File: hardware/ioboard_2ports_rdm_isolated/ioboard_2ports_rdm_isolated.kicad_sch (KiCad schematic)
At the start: 30 parts, among them J1 Conn_02x06_Odd_Even, J12 Conn_01x03, J2 XLR3, J3 XLR3, J6 Conn_01x03, J8 XLR3, J9 XLR3, U1 M24C64-RMN6TP, U2 CRE1S0505DC, U4 ADM2483xRW, U6 ADM2483xRW

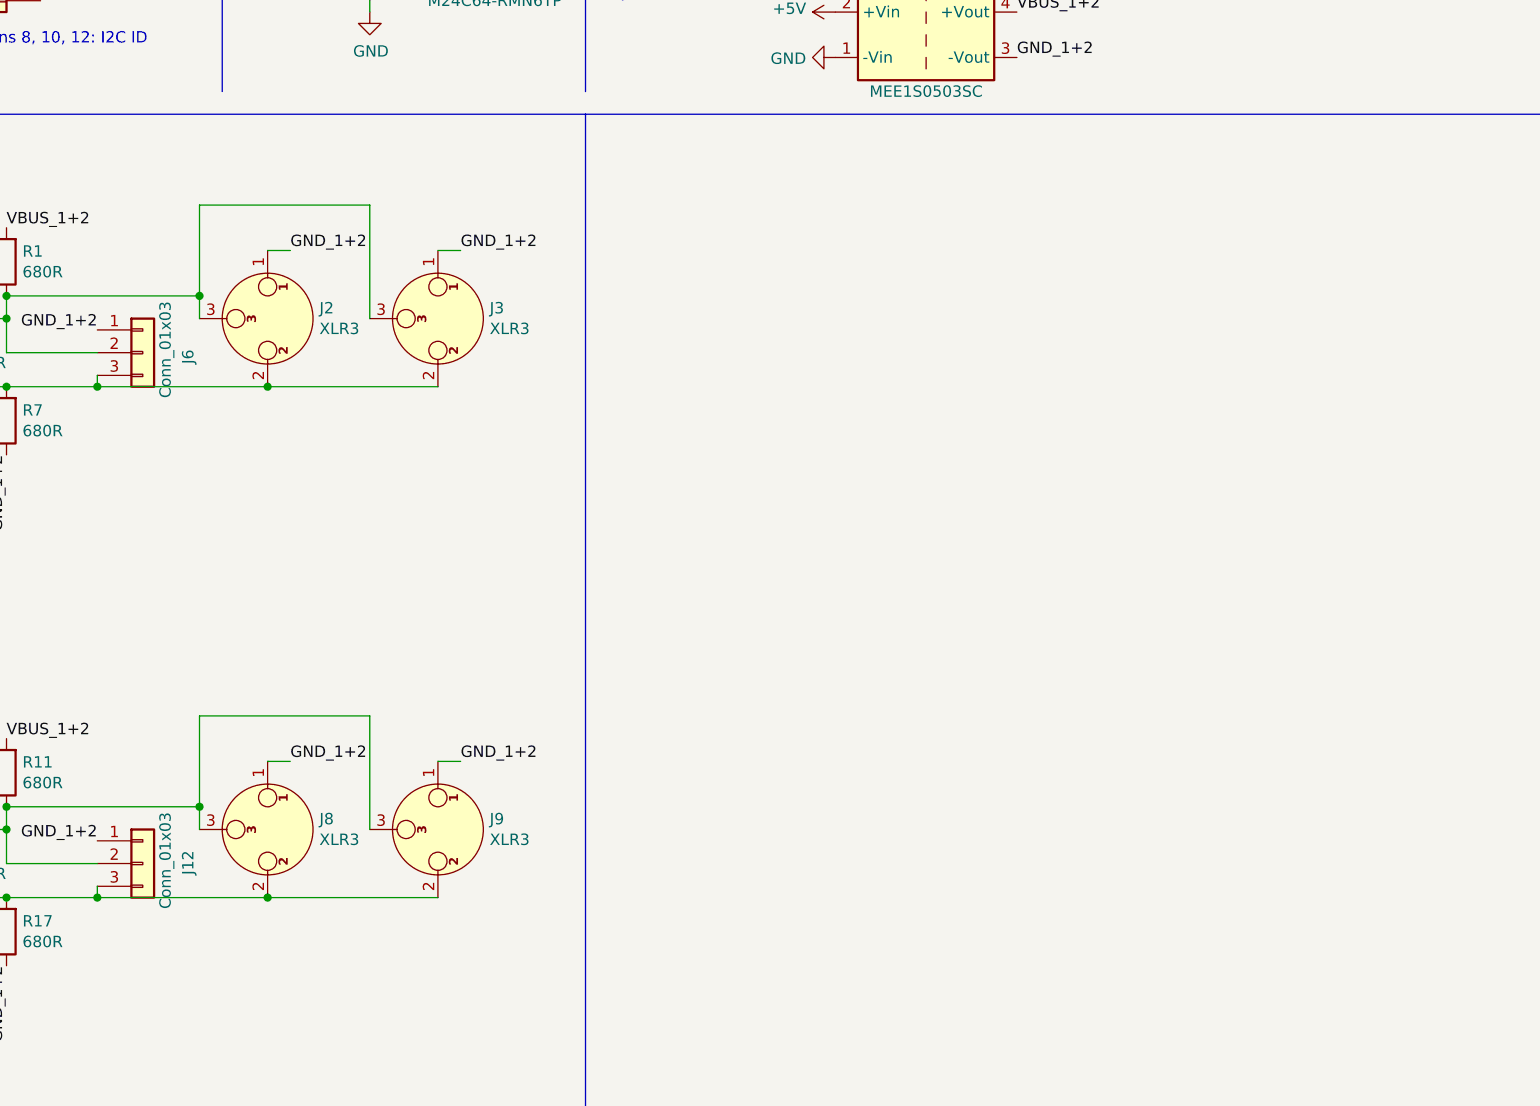
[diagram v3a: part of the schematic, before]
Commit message: Add an RJ45 connector to ioboard_2ports_rdm_isolated
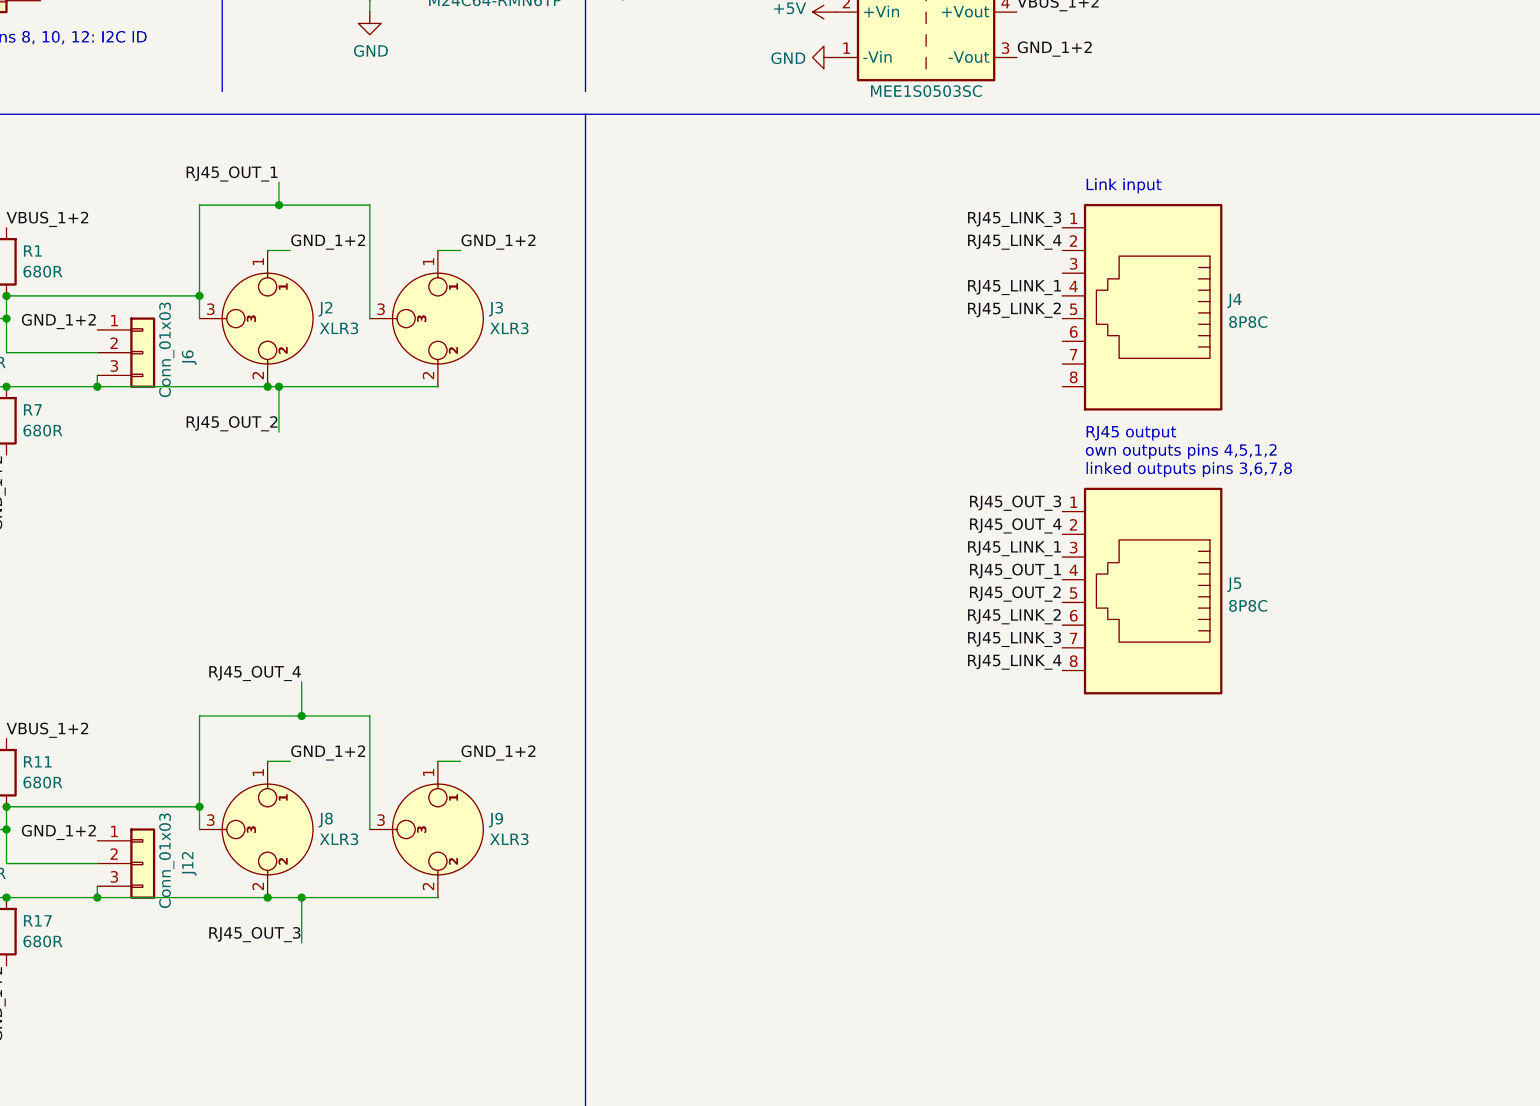
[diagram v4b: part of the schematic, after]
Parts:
- added J4, J5: 8P8C, Connector_RJ:RJ45_Amphenol_RJHSE5380, symbol Connector:8P8C
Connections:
- net RJ45_OUT_1: now reaches J2.3, J3.3, J6.2 (Pin_2), R1.1, R5.2, U4.12 (A)
- net RJ45_OUT_1: now also J5.4
- net RJ45_OUT_2: now reaches J2.2, J3.2, J6.3 (Pin_3), R5.1, R7.2, U4.13 (B)
- net RJ45_OUT_2: now also J5.5
- net RJ45_OUT_3: now reaches J12.3 (Pin_3), J8.2, J9.2, R15.1, R17.2, U6.13 (B)
- net RJ45_OUT_3: now also J5.1
- net RJ45_OUT_4: now reaches J12.2 (Pin_2), J8.3, J9.3, R11.1, R15.2, U6.12 (A)
- net RJ45_OUT_4: now also J5.2
- new net RJ45_LINK_1: J4.4, J5.3
- new net RJ45_LINK_2: J4.5, J5.6
- new net RJ45_LINK_3: J4.1, J5.7
- new net RJ45_LINK_4: J4.2, J5.8
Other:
- note added: "Link input"
- note added: "RJ45 output own outputs pins 4,5,1,2 linked outputs pins 3,6,7,8"
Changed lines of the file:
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@@
     (title "rp2040_dongle_ioboard_2ports_rdm_isolated")
     (date "2022-11-09")
-    (rev "0.5")
+    (rev "0.6")
     (company "https://www.openlighting.org")
   )
   (junction (at 105.41 73.66) (diameter 0) (color 0 0 0 0)
   )
+  (junction (at 114.3 83.82) (diameter 0) (color 0 0 0 0)
+  )
   (junction (at 113.03 83.82) (diameter 0) (color 0 0 0 0)
   )
@@
   (junction (at 45.72 64.77) (diameter 0) (color 0 0 0 0)
   )
+  (junction (at 114.3 63.5) (diameter 0) (color 0 0 0 0)
+  )
   (junction (at 29.21 139.7) (diameter 0) (color 0 0 0 0)
   )
@@
   (junction (at 77.47 83.82) (diameter 0) (color 0 0 0 0)
   )
+  (junction (at 116.84 140.97) (diameter 0) (color 0 0 0 0)
+  )
   (junction (at 83.82 73.66) (diameter 0) (color 0 0 0 0)
   )
@@
   (junction (at 83.82 83.82) (diameter 0) (color 0 0 0 0)
   )
+  (junction (at 116.84 120.65) (diameter 0) (color 0 0 0 0)
+  )
   (junction (at 45.72 121.92) (diameter 0) (color 0 0 0 0)
   )
@@
     (stroke (width 0) (type default) (color 0 0 0 0))
   )
-  (wire (pts (xy 105.41 120.65) (xy 124.46 120.65))
+  (wire (pts (xy 105.41 120.65) (xy 116.84 120.65))
     (stroke (width 0) (type default) (color 0 0 0 0))
   )
@@
     (stroke (width 0) (type default) (color 0 0 0 0))
   )
-  (wire (pts (xy 105.41 63.5) (xy 124.46 63.5))
+  (wire (pts (xy 105.41 63.5) (xy 114.3 63.5))
     (stroke (width 0) (type default) (color 0 0 0 0))
   )
@@
     (stroke (width 0) (type default) (color 0 0 0 0))
   )
+  (wire (pts (xy 116.84 140.97) (xy 132.08 140.97))
+    (stroke (width 0) (type default) (color 0 0 0 0))
+  )
   (wire (pts (xy 66.04 134.62) (xy 71.12 134.62))
     (stroke (width 0) (type default) (color 0 0 0 0))
@@
     (stroke (width 0) (type default) (color 0 0 0 0))
   )
+  (wire (pts (xy 116.84 116.84) (xy 116.84 120.65))
+    (stroke (width 0) (type default) (color 0 0 0 0))
+  )
   (wire (pts (xy 24.13 72.39) (xy 21.59 72.39))
     (stroke (width 0) (type default) (color 0 0 0 0))
   )
+  (wire (pts (xy 114.3 83.82) (xy 114.3 88.9))
+    (stroke (width 0) (type default) (color 0 0 0 0))
+  )
   (wire (pts (xy 124.46 63.5) (xy 124.46 76.2))
     (stroke (width 0) (type default) (color 0 0 0 0))
@@
     (stroke (width 0) (type default) (color 0 0 0 0))
   )
+  (wire (pts (xy 116.84 120.65) (xy 124.46 120.65))
+    (stroke (width 0) (type default) (color 0 0 0 0))
+  )
   (wire (pts (xy 173.99 24.13) (xy 173.99 22.86))
     (stroke (width 0) (type default) (color 0 0 0 0))
@@
     (stroke (width 0) (type default) (color 0 0 0 0))
   )
+  (wire (pts (xy 114.3 83.82) (xy 132.08 83.82))
+    (stroke (width 0) (type default) (color 0 0 0 0))
+  )
+  (wire (pts (xy 114.3 60.96) (xy 114.3 63.5))
+    (stroke (width 0) (type default) (color 0 0 0 0))
+  )
   (wire (pts (xy 66.04 139.7) (xy 71.12 139.7))
     (stroke (width 0) (type default) (color 0 0 0 0))
@@
     (stroke (width 0) (type default) (color 0 0 0 0))
   )
+  (wire (pts (xy 116.84 140.97) (xy 116.84 146.05))
+    (stroke (width 0) (type default) (color 0 0 0 0))
+  )
   (wire (pts (xy 77.47 76.2) (xy 83.82 76.2))
     (stroke (width 0) (type default) (color 0 0 0 0))
   )
+  (wire (pts (xy 114.3 63.5) (xy 124.46 63.5))
+    (stroke (width 0) (type default) (color 0 0 0 0))
+  )
   (wire (pts (xy 113.03 68.58) (xy 115.57 68.58))
     (stroke (width 0) (type default) (color 0 0 0 0))
   )
-  (wire (pts (xy 113.03 140.97) (xy 132.08 140.97))
+  (wire (pts (xy 113.03 140.97) (xy 116.84 140.97))
     (stroke (width 0) (type default) (color 0 0 0 0))
   )
@@
     (stroke (width 0) (type default) (color 0 0 0 0))
   )
-  (wire (pts (xy 113.03 83.82) (xy 132.08 83.82))
+  (wire (pts (xy 113.03 83.82) (xy 114.3 83.82))
     (stroke (width 0) (type default) (color 0 0 0 0))
   )
@@
     (effects (font (size 1.27 1.27)) (justify left bottom))
   )
+  (text "Link input" (at 204.47 62.23 0)
+    (effects (font (size 1.27 1.27)) (justify left bottom))
+  )
+  (text "RJ45 output\nown outputs pins 4,5,1,2\nlinked outputs pins 3,6,7,8"
+    (at 204.47 93.98 0)
+    (effects (font (size 1.27 1.27)) (justify left bottom))
+  )
   (text "Two footprints are\nsupported. Mount\nonly one converter!"
     (at 149.86 40.64 0)
@@
     (effects (font (size 1.27 1.27)) (justify left bottom))
   )
+  (label "RJ45_OUT_3" (at 116.84 146.05 180)
+    (effects (font (size 1.27 1.27)) (justify right bottom))
+  )
   (label "GND_1+2" (at 55.88 157.48 0)
     (effects (font (size 1.27 1.27)) (justify left bottom))
@@
     (effects (font (size 1.27 1.27)) (justify left bottom))
   )
+  (label "RJ45_OUT_3" (at 201.93 97.79 180)
+    (effects (font (size 1.27 1.27)) (justify right bottom))
+  )
+  (label "RJ45_OUT_1" (at 114.3 60.96 180)
+    (effects (font (size 1.27 1.27)) (justify right bottom))
+  )
   (label "ID1" (at 114.3 33.02 180)
     (effects (font (size 1.27 1.27)) (justify right bottom))
@@
     (effects (font (size 1.27 1.27)) (justify right bottom))
   )
+  (label "RJ45_OUT_4" (at 201.93 100.33 180)
+    (effects (font (size 1.27 1.27)) (justify right bottom))
+  )
   (label "ID0" (at 114.3 30.48 180)
     (effects (font (size 1.27 1.27)) (justify right bottom))
@@
     (effects (font (size 1.27 1.27)) (justify right bottom))
   )
+  (label "RJ45_LINK_3" (at 201.93 113.03 180)
+    (effects (font (size 1.27 1.27)) (justify right bottom))
+  )
   (label "GP1" (at 21.59 72.39 180)
     (effects (font (size 1.27 1.27)) (justify right bottom))
@@
     (effects (font (size 1.27 1.27)) (justify left bottom))
   )
+  (label "RJ45_OUT_2" (at 114.3 88.9 180)
+    (effects (font (size 1.27 1.27)) (justify right bottom))
+  )
   (label "GND_1+2" (at 93.98 77.47 180)
     (effects (font (size 1.27 1.27)) (justify right bottom))
@@
     (effects (font (size 1.27 1.27)) (justify right bottom))
   )
+  (label "RJ45_LINK_1" (at 201.93 73.66 180)
+    (effects (font (size 1.27 1.27)) (justify right bottom))
+  )
+  (label "RJ45_LINK_3" (at 201.93 66.04 180)
+    (effects (font (size 1.27 1.27)) (justify right bottom))
+  )
   (label "VBUS_1+2" (at 199.39 22.86 0)
     (effects (font (size 1.27 1.27)) (justify left bottom))
@@
     (effects (font (size 1.27 1.27)) (justify right bottom))
   )
+  (label "RJ45_OUT_1" (at 201.93 105.41 180)
+    (effects (font (size 1.27 1.27)) (justify right bottom))
+  )
+  (label "RJ45_LINK_4" (at 201.93 115.57 180)
+    (effects (font (size 1.27 1.27)) (justify right bottom))
+  )
   (label "GND_1+2" (at 83.82 91.44 270)
     (effects (font (size 1.27 1.27)) (justify right bottom))
   )
+  (label "RJ45_LINK_1" (at 201.93 102.87 180)
+    (effects (font (size 1.27 1.27)) (justify right bottom))
+  )
   (label "VBUS_1+2" (at 196.85 41.91 0)
     (effects (font (size 1.27 1.27)) (justify left bottom))
@@
     (effects (font (size 1.27 1.27)) (justify left bottom))
   )
+  (label "RJ45_LINK_2" (at 201.93 76.2 180)
+    (effects (font (size 1.27 1.27)) (justify right bottom))
+  )
   (label "ID0" (at 87.63 35.56 0)
     (effects (font (size 1.27 1.27)) (justify left bottom))
   )
+  (label "RJ45_LINK_4" (at 201.93 68.58 180)
+    (effects (font (size 1.27 1.27)) (justify right bottom))
+  )
+  (label "RJ45_OUT_4" (at 116.84 116.84 180)
+    (effects (font (size 1.27 1.27)) (justify right bottom))
+  )
   (label "GND_1+2" (at 115.57 125.73 0)
     (effects (font (size 1.27 1.27)) (justify left bottom))
@@
     (effects (font (size 1.27 1.27)) (justify left bottom))
   )
+  (label "RJ45_OUT_2" (at 201.93 107.95 180)
+    (effects (font (size 1.27 1.27)) (justify right bottom))
+  )
   (label "GND_1+2" (at 93.98 134.62 180)
     (effects (font (size 1.27 1.27)) (justify right bottom))
   )
   (label "GP2" (at 74.93 35.56 180)
+    (effects (font (size 1.27 1.27)) (justify right bottom))
+  )
+  (label "RJ45_LINK_2" (at 201.93 110.49 180)
     (effects (font (size 1.27 1.27)) (justify right bottom))
   )
@@
     (pin "3")
   )
+  (symbol (lib_id "Connector:8P8C") (at 212.09 73.66 180) (unit 1)
+    (in_bom yes) (on_board yes) (fields_autoplaced)
+    (property "Reference" "J4" (id 0) (at 220.472 74.0953 0)
+      (effects (font (size 1.27 1.27)) (justify right))
+    )
+    (property "Value" "8P8C" (id 1) (at 220.472 76.6322 0)
+      (effects (font (size 1.27 1.27)) (justify right))
+    )
+    (property "Footprint" "Connector_RJ:RJ45_Amphenol_RJHSE5380" (id 2) (at 212.09 74.295 90)
+      (effects (font (size 1.27 1.27)) hide)
+    )
+    (property "Datasheet" "~" (id 3) (at 212.09 74.295 90)
+      (effects (font (size 1.27 1.27)) hide)
+    )
+    (pin "1")
+    (pin "2")
+    (pin "3")
+    (pin "4")
+    (pin "5")
+    (pin "6")
+    (pin "7")
+    (pin "8")
+  )
+  (symbol (lib_id "Connector:8P8C") (at 212.09 105.41 180) (unit 1)
+    (in_bom yes) (on_board yes) (fields_autoplaced)
+    (property "Reference" "J5" (id 0) (at 220.472 105.8453 0)
+      (effects (font (size 1.27 1.27)) (justify right))
+    )
+    (property "Value" "8P8C" (id 1) (at 220.472 108.3822 0)
+      (effects (font (size 1.27 1.27)) (justify right))
+    )
+    (property "Footprint" "Connector_RJ:RJ45_Amphenol_RJHSE5380" (id 2) (at 212.09 106.045 90)
+      (effects (font (size 1.27 1.27)) hide)
+    )
+    (property "Datasheet" "~" (id 3) (at 212.09 106.045 90)
+      (effects (font (size 1.27 1.27)) hide)
+    )
+    (pin "1")
+    (pin "2")
+    (pin "3")
+    (pin "4")
+    (pin "5")
+    (pin "6")
+    (pin "7")
+    (pin "8")
+  )
   (sheet_instances
     (path "/" (page "1"))
@@
       (reference "J3") (unit 1) (value "XLR3") (footprint "NC3FD-H:Jack_XLR_Neutrik_NC3FD-H_Horizontal")
     )
+    (path "/00cad9ac-2b14-4956-a62a-c9828ff3e0c0"
+      (reference "J4") (unit 1) (value "8P8C") (footprint "Connector_RJ:RJ45_Amphenol_RJHSE5380")
+    )
+    (path "/51a341f4-726a-4ff1-9c8e-5fb0ba36a59e"
+      (reference "J5") (unit 1) (value "8P8C") (footprint "Connector_RJ:RJ45_Amphenol_RJHSE5380")
+    )
     (path "/00000000-0000-0000-0000-00006059f495"

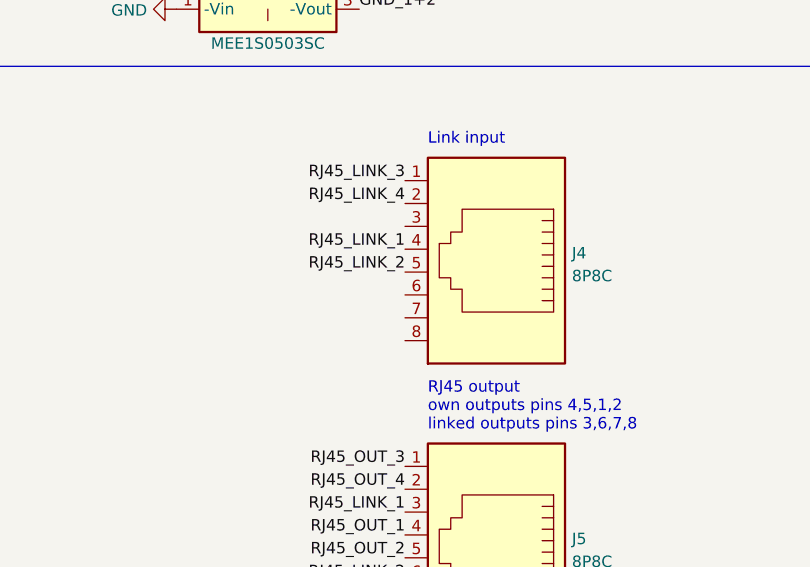
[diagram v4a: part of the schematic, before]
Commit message: Replace Amphenol's RJ45 by the one by Sparkfun/4UCON
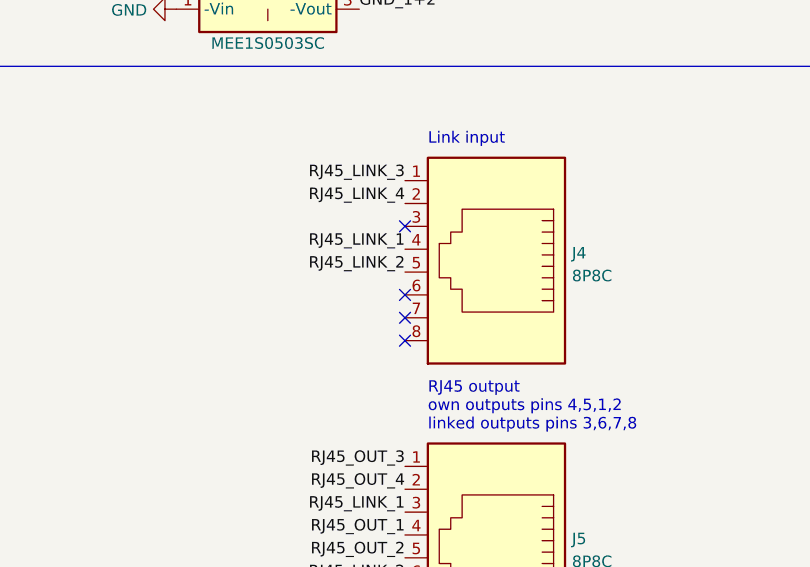
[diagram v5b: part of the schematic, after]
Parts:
- J4, J5: footprint Connector_RJ:RJ45_Amphenol_RJHSE5380 -> RJ45_Sparkfun:RJ45_Sparkfun
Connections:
- no-connect marks 0 -> 4
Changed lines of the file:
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@@
   (junction (at 105.41 130.81) (diameter 0) (color 0 0 0 0)
   )
+  (no_connect (at 201.93 83.82))
+  (no_connect (at 201.93 78.74))
+  (no_connect (at 201.93 81.28))
+  (no_connect (at 201.93 71.12))
   (polyline (pts (xy 12.7 53.34) (xy 284.48 53.34))
     (stroke (width 0) (type default) (color 0 0 0 0))
@@
       (effects (font (size 1.27 1.27)) (justify right))
     )
-    (property "Footprint" "Connector_RJ:RJ45_Amphenol_RJHSE5380" (id 2) (at 212.09 74.295 90)
+    (property "Footprint" "RJ45_Sparkfun:RJ45_Sparkfun" (id 2) (at 212.09 74.295 90)
       (effects (font (size 1.27 1.27)) hide)
     )
@@
       (effects (font (size 1.27 1.27)) (justify right))
     )
-    (property "Footprint" "Connector_RJ:RJ45_Amphenol_RJHSE5380" (id 2) (at 212.09 106.045 90)
+    (property "Footprint" "RJ45_Sparkfun:RJ45_Sparkfun" (id 2) (at 212.09 106.045 90)
       (effects (font (size 1.27 1.27)) hide)
     )
@@
     )
     (path "/00cad9ac-2b14-4956-a62a-c9828ff3e0c0"
-      (reference "J4") (unit 1) (value "8P8C") (footprint "Connector_RJ:RJ45_Amphenol_RJHSE5380")
+      (reference "J4") (unit 1) (value "8P8C") (footprint "RJ45_Sparkfun:RJ45_Sparkfun")
     )
     (path "/51a341f4-726a-4ff1-9c8e-5fb0ba36a59e"
-      (reference "J5") (unit 1) (value "8P8C") (footprint "Connector_RJ:RJ45_Amphenol_RJHSE5380")
+      (reference "J5") (unit 1) (value "8P8C") (footprint "RJ45_Sparkfun:RJ45_Sparkfun")
     )
     (path "/00000000-0000-0000-0000-00006059f495"

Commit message: Hardware: Fix one IC order code (was 2kbit EEPROM instead of 64kbit ....)
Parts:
- U1: LCSC C7562 -> C79988
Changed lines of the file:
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@@
       (effects (font (size 1.27 1.27)) hide)
     )
-    (property "LCSC" "C7562" (id 4) (at 124.46 33.02 0)
+    (property "LCSC" "C79988" (id 4) (at 124.46 33.02 0)
       (effects (font (size 1.27 1.27)) hide)
     )
